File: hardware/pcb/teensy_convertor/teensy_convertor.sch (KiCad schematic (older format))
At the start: 2 parts, among them U1 Teensy-3.2

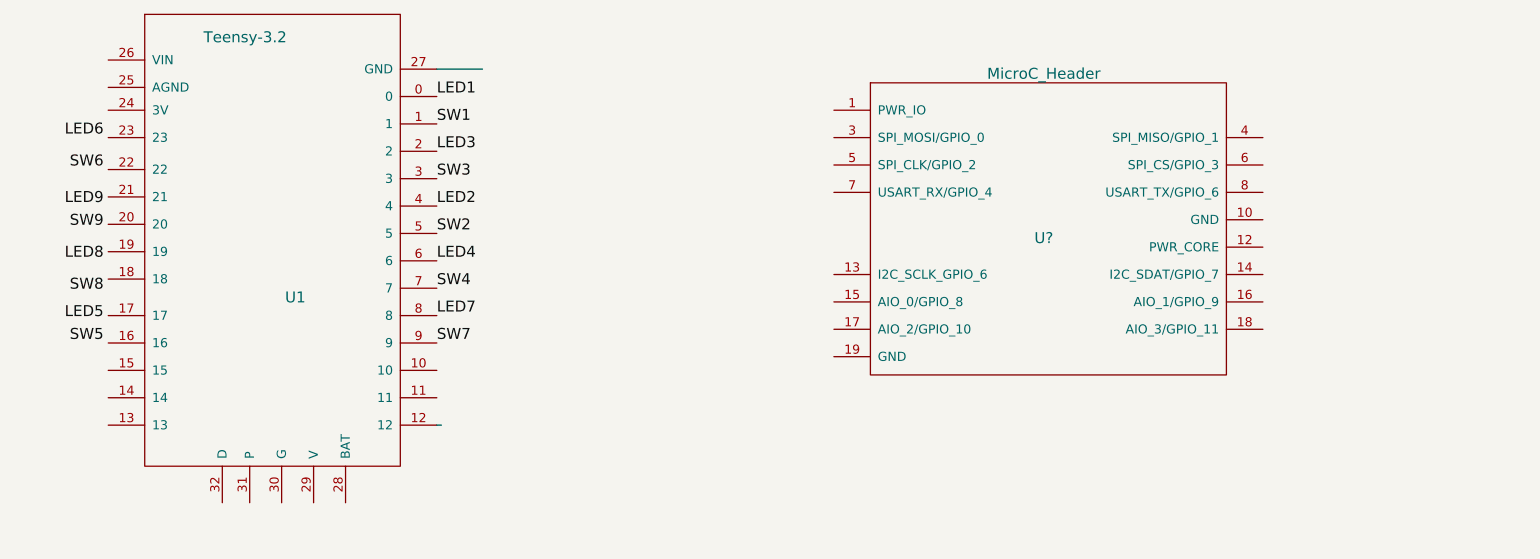
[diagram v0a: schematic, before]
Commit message: Add lables from Teensy to microcontroller header
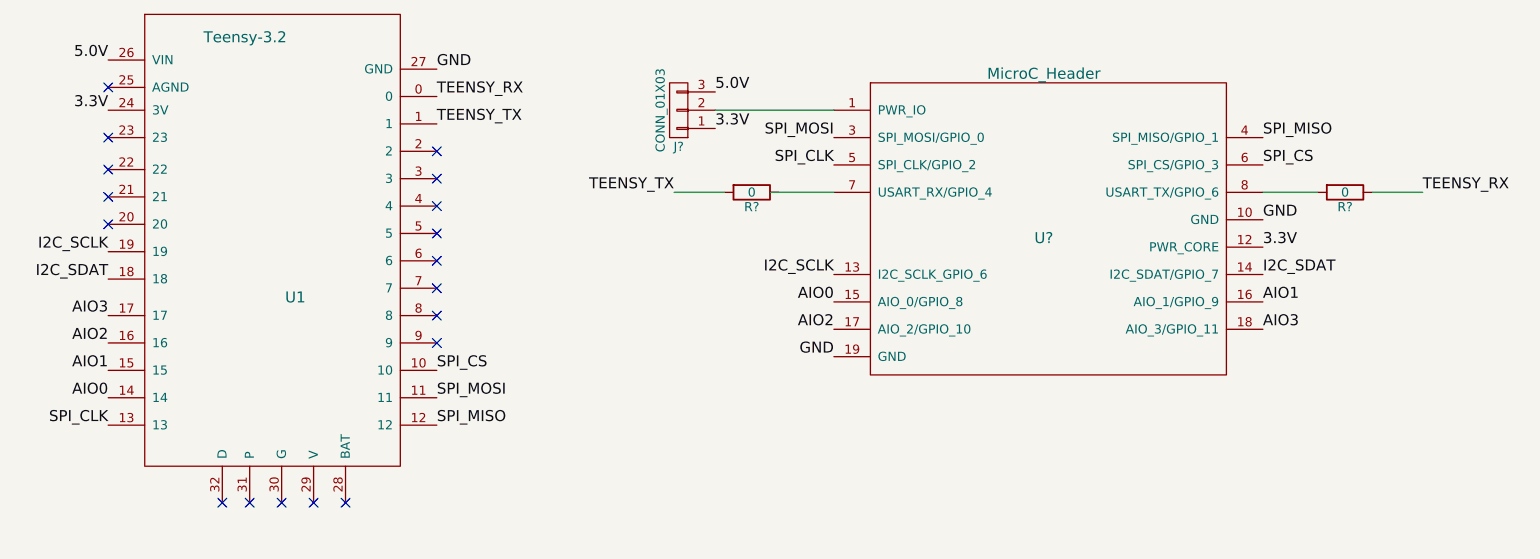
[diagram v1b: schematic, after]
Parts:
- added J?: CONN_01X03, symbol CONN_01X03
- added R? (x2): 0, symbol R
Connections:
- net labels added: 3.3V, 5.0V, AIO0, AIO1, AIO2, AIO3, GND, I2C_SCLK, I2C_SDAT, SPI_CLK, SPI_CS, SPI_MISO, SPI_MOSI, TEENSY_RX, TEENSY_TX
- net labels removed: LED1, LED2, LED3, LED4, LED5, LED6, LED7, LED8, LED9, SW1, SW2, SW3, SW4, SW5, SW6, SW7, SW8, SW9
- wire segments 2 -> 5
- no-connect marks 0 -> 18
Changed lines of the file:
@@
 LIBS:Zilog
 LIBS:micro_c_header
+LIBS:teensy_convertor-cache
 EELAYER 25 0
 EELAYER END
@@
 	1    0    0    -1
 $EndComp
-Wire Wire Line
-	4175 2625 3925 2625
-Wire Wire Line
-	3950 4575 3925 4575
-Text Label 3925 2775 0    60   ~ 0
-LED1
-Text Label 3925 2925 0    60   ~ 0
-SW1
-Text Label 3925 3075 0    60   ~ 0
-LED3
-Text Label 3925 3225 0    60   ~ 0
-SW3
-Text Label 3925 3375 0    60   ~ 0
-LED2
-Text Label 3925 3525 0    60   ~ 0
-SW2
-Text Label 2100 3000 2    60   ~ 0
-LED6
-Text Label 2100 3175 2    60   ~ 0
-SW6
-Text Label 2100 3375 2    60   ~ 0
-LED9
-Text Label 2100 3500 2    60   ~ 0
-SW9
-Text Label 2100 3675 2    60   ~ 0
-LED8
-Text Label 2100 3850 2    60   ~ 0
-SW8
-Text Label 3925 3675 0    60   ~ 0
-LED4
-Text Label 3925 3825 0    60   ~ 0
-SW4
-Text Label 3925 3975 0    60   ~ 0
-LED7
-Text Label 3925 4125 0    60   ~ 0
-SW7
-Text Label 2100 4000 2    60   ~ 0
-LED5
-Text Label 2100 4125 2    60   ~ 0
-SW5
 $Comp
 L MicroC_Header U?
@@
 	1    0    0    -1
 $EndComp
+$Comp
+L CONN_01X03 J?
+U 1 1 592B3FA3
+P 5250 2850
+F 0 "J?" H 5250 3050 50  0000 C CNN
+F 1 "CONN_01X03" V 5350 2850 50  0000 C CNN
+F 2 "" H 5250 2850 50  0001 C CNN
+F 3 "" H 5250 2850 50  0001 C CNN
+	1    5250 2850
+	-1   0    0    1
+$EndComp
+Text Label 2125 2850 2    60   ~ 0
+3.3V
+Text Label 5450 2950 0    60   ~ 0
+3.3V
+Text Label 8450 3600 0    60   ~ 0
+3.3V
+Text Label 2125 2575 2    60   ~ 0
+5.0V
+Text Label 5450 2750 0    60   ~ 0
+5.0V
+Text Label 8450 3450 0    60   ~ 0
+GND
+Text Label 6100 4200 2    60   ~ 0
+GND
+Text Label 3925 2625 0    60   ~ 0
+GND
+Text Label 6100 3000 2    60   ~ 0
+SPI_MOSI
+Text Label 3925 4425 0    60   ~ 0
+SPI_MOSI
+Text Label 6100 3150 2    60   ~ 0
+SPI_CLK
+Text Label 2125 4575 2    60   ~ 0
+SPI_CLK
+Text Label 8450 3000 0    60   ~ 0
+SPI_MISO
+Text Label 3925 4575 0    60   ~ 0
+SPI_MISO
+Text Label 8450 3150 0    60   ~ 0
+SPI_CS
+Text Label 3925 4275 0    60   ~ 0
+SPI_CS
+$Comp
+L R R?
+U 1 1 592B478D
+P 5650 3300
+F 0 "R?" V 5730 3300 50  0000 C CNN
+F 1 "0" V 5650 3300 50  0000 C CNN
+F 2 "" V 5580 3300 50  0001 C CNN
+F 3 "" H 5650 3300 50  0001 C CNN
+	1    5650 3300
+	0    1    1    0
+$EndComp
+$Comp
+L R R?
+U 1 1 592B4823
+P 8900 3300
+F 0 "R?" V 8980 3300 50  0000 C CNN
+F 1 "0" V 8900 3300 50  0000 C CNN
+F 2 "" V 8830 3300 50  0001 C CNN
+F 3 "" H 8900 3300 50  0001 C CNN
+	1    8900 3300
+	0    1    1    0
+$EndComp
+Wire Wire Line
+	6100 2850 5450 2850
+Wire Wire Line
+	5750 3300 6100 3300
+Wire Wire Line
+	8450 3300 8750 3300
+Wire Wire Line
+	9050 3300 9325 3300
+Wire Wire Line
+	5500 3300 5225 3300
+Text Label 9325 3300 0    60   ~ 0
+TEENSY_RX
+Text Label 3925 2775 0    60   ~ 0
+TEENSY_RX
+Text Label 5225 3300 2    60   ~ 0
+TEENSY_TX
+Text Label 3925 2925 0    60   ~ 0
+TEENSY_TX
+Text Label 6100 3750 2    60   ~ 0
+I2C_SCLK
+Text Label 2125 3625 2    60   ~ 0
+I2C_SCLK
+Text Label 2125 3775 2    60   ~ 0
+I2C_SDAT
+Text Label 8450 3750 0    60   ~ 0
+I2C_SDAT
+Text Label 6100 3900 2    60   ~ 0
+AIO0
+Text Label 2125 4425 2    60   ~ 0
+AIO0
+Text Label 6100 4050 2    60   ~ 0
+AIO2
+Text Label 8450 3900 0    60   ~ 0
+AIO1
+Text Label 8450 4050 0    60   ~ 0
+AIO3
+Text Label 2125 4125 2    60   ~ 0
+AIO2
+Text Label 2125 4275 2    60   ~ 0
+AIO1
+Text Label 2125 3975 2    60   ~ 0
+AIO3
+NoConn ~ 3925 3075
+NoConn ~ 3925 3225
+NoConn ~ 3925 3375
+NoConn ~ 3925 3525
+NoConn ~ 3925 3675
+NoConn ~ 3925 3825
+NoConn ~ 3925 3975
+NoConn ~ 3925 4125
+NoConn ~ 3425 5000
+NoConn ~ 3250 5000
+NoConn ~ 3075 5000
+NoConn ~ 2900 5000
+NoConn ~ 2750 5000
+NoConn ~ 2125 3475
+NoConn ~ 2125 3325
+NoConn ~ 2125 3175
+NoConn ~ 2125 3000
+NoConn ~ 2125 2725
 $EndSCHEMATC

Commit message: Initial association and import into the layout tool
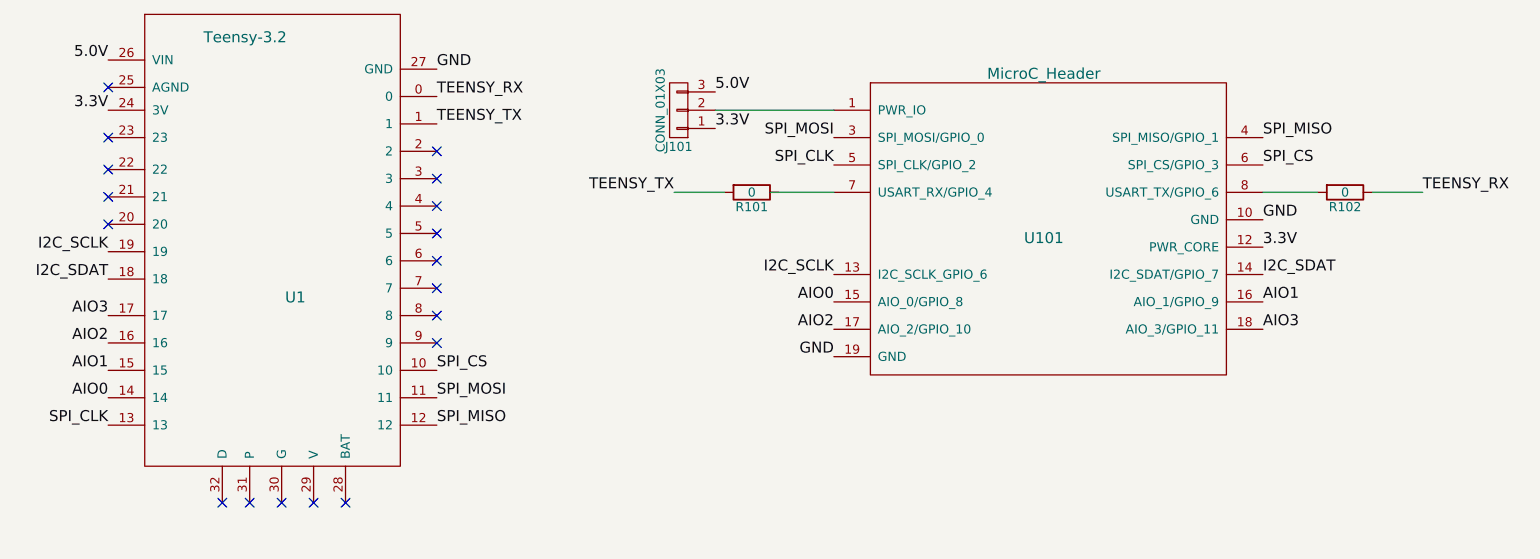
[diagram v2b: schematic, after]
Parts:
- J101: renamed from J?; footprint (none) -> Pin_Headers:Pin_Header_Straight_1x03_Pitch2.54mm
- R101, R102: renamed from R?; footprint (none) -> Resistors_SMD:R_0805_HandSoldering
- U1: footprint Key:Teensy-32 -> teensy_convertor:Teensy-32
- U101: renamed from U?; footprint (none) -> micro_c_header:MicroC_Header_Pitch2.54mm
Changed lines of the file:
@@
 F 0 "U1" H 3150 3375 60  0000 C CNN
 F 1 "Teensy-3.2" H 2875 4800 60  0000 C CNN
-F 2 "Key:Teensy-32" H 2775 3300 60  0001 C CNN
+F 2 "teensy_convertor:Teensy-32" H 2775 3300 60  0001 C CNN
 F 3 "" H 2775 3300 60  0001 C CNN
 	1    3000 3625
@@
 $EndComp
 $Comp
-L MicroC_Header U?
+L MicroC_Header U101
 U 1 1 59279C22
 P 7250 3550
-F 0 "U?" H 7250 3550 60  0000 C CNN
+F 0 "U101" H 7250 3550 60  0000 C CNN
 F 1 "MicroC_Header" H 7250 4450 60  0000 C CNN
-F 2 "" H 7250 3400 60  0001 C CNN
+F 2 "micro_c_header:MicroC_Header_Pitch2.54mm" H 7250 3400 60  0001 C CNN
 F 3 "" H 7250 3400 60  0001 C CNN
 	1    7250 3550
@@
 $EndComp
 $Comp
-L CONN_01X03 J?
+L CONN_01X03 J101
 U 1 1 592B3FA3
 P 5250 2850
-F 0 "J?" H 5250 3050 50  0000 C CNN
+F 0 "J101" H 5250 3050 50  0000 C CNN
 F 1 "CONN_01X03" V 5350 2850 50  0000 C CNN
-F 2 "" H 5250 2850 50  0001 C CNN
+F 2 "Pin_Headers:Pin_Header_Straight_1x03_Pitch2.54mm" H 5250 2850 50  0001 C CNN
 F 3 "" H 5250 2850 50  0001 C CNN
 	1    5250 2850
@@
 SPI_CS
 $Comp
-L R R?
+L R R101
 U 1 1 592B478D
 P 5650 3300
-F 0 "R?" V 5730 3300 50  0000 C CNN
+F 0 "R101" V 5730 3300 50  0000 C CNN
 F 1 "0" V 5650 3300 50  0000 C CNN
-F 2 "" V 5580 3300 50  0001 C CNN
+F 2 "Resistors_SMD:R_0805_HandSoldering" V 5580 3300 50  0001 C CNN
 F 3 "" H 5650 3300 50  0001 C CNN
 	1    5650 3300
@@
 $EndComp
 $Comp
-L R R?
+L R R102
 U 1 1 592B4823
 P 8900 3300
-F 0 "R?" V 8980 3300 50  0000 C CNN
+F 0 "R102" V 8980 3300 50  0000 C CNN
 F 1 "0" V 8900 3300 50  0000 C CNN
-F 2 "" V 8830 3300 50  0001 C CNN
+F 2 "Resistors_SMD:R_0805_HandSoldering" V 8830 3300 50  0001 C CNN
 F 3 "" H 8900 3300 50  0001 C CNN
 	1    8900 3300

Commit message: Initial layout
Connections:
- no-connect marks 18 -> 17
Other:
- moved on the sheet: U1
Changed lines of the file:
@@
 L Teensy-3.2 U1
 U 1 1 586B0354
-P 3000 3625
-F 0 "U1" H 3150 3375 60  0000 C CNN
-F 1 "Teensy-3.2" H 2875 4800 60  0000 C CNN
-F 2 "teensy_convertor:Teensy-32" H 2775 3300 60  0001 C CNN
-F 3 "" H 2775 3300 60  0001 C CNN
-	1    3000 3625
-	1    0    0    -1
+P 3100 3625
+F 0 "U1" H 3250 3375 60  0000 C CNN
+F 1 "Teensy-3.2" H 2975 4800 60  0000 C CNN
+F 2 "teensy_convertor:Teensy-32" H 2875 3300 60  0001 C CNN
+F 3 "" H 2875 3300 60  0001 C CNN
+	1    3100 3625
+	-1   0    0    -1
 $EndComp
 $Comp
@@
 	-1   0    0    1
 $EndComp
-Text Label 2125 2850 2    60   ~ 0
+Text Label 3975 2850 0    60   ~ 0
 3.3V
 Text Label 5450 2950 0    60   ~ 0
@@
 Text Label 8450 3600 0    60   ~ 0
 3.3V
-Text Label 2125 2575 2    60   ~ 0
+Text Label 3975 2575 0    60   ~ 0
 5.0V
 Text Label 5450 2750 0    60   ~ 0
@@
 Text Label 6100 4200 2    60   ~ 0
 GND
-Text Label 3925 2625 0    60   ~ 0
+Text Label 2175 2625 2    60   ~ 0
 GND
 Text Label 6100 3000 2    60   ~ 0
 SPI_MOSI
-Text Label 3925 4425 0    60   ~ 0
+Text Label 2175 4425 2    60   ~ 0
 SPI_MOSI
 Text Label 6100 3150 2    60   ~ 0
 SPI_CLK
-Text Label 2125 4575 2    60   ~ 0
+Text Label 3975 4575 0    60   ~ 0
 SPI_CLK
 Text Label 8450 3000 0    60   ~ 0
 SPI_MISO
-Text Label 3925 4575 0    60   ~ 0
+Text Label 2175 4575 2    60   ~ 0
 SPI_MISO
 Text Label 8450 3150 0    60   ~ 0
 SPI_CS
-Text Label 3925 4275 0    60   ~ 0
+Text Label 2175 4275 2    60   ~ 0
 SPI_CS
 $Comp
@@
 	6100 2850 5450 2850
 Wire Wire Line
-	5750 3300 6100 3300
+	5800 3300 6100 3300
 Wire Wire Line
 	8450 3300 8750 3300
@@
 Text Label 9325 3300 0    60   ~ 0
 TEENSY_RX
-Text Label 3925 2775 0    60   ~ 0
+Text Label 2175 2775 2    60   ~ 0
 TEENSY_RX
 Text Label 5225 3300 2    60   ~ 0
 TEENSY_TX
-Text Label 3925 2925 0    60   ~ 0
+Text Label 2175 2925 2    60   ~ 0
 TEENSY_TX
 Text Label 6100 3750 2    60   ~ 0
 I2C_SCLK
-Text Label 2125 3625 2    60   ~ 0
+Text Label 3975 3625 0    60   ~ 0
 I2C_SCLK
-Text Label 2125 3775 2    60   ~ 0
+Text Label 3975 3775 0    60   ~ 0
 I2C_SDAT
 Text Label 8450 3750 0    60   ~ 0
@@
 Text Label 6100 3900 2    60   ~ 0
 AIO0
-Text Label 2125 4425 2    60   ~ 0
+Text Label 3975 4425 0    60   ~ 0
 AIO0
 Text Label 6100 4050 2    60   ~ 0
@@
 Text Label 8450 4050 0    60   ~ 0
 AIO3
-Text Label 2125 4125 2    60   ~ 0
+Text Label 3975 4125 0    60   ~ 0
 AIO2
-Text Label 2125 4275 2    60   ~ 0
+Text Label 3975 4275 0    60   ~ 0
 AIO1
-Text Label 2125 3975 2    60   ~ 0
+Text Label 3975 3975 0    60   ~ 0
 AIO3
-NoConn ~ 3925 3075
-NoConn ~ 3925 3225
-NoConn ~ 3925 3375
-NoConn ~ 3925 3525
-NoConn ~ 3925 3675
-NoConn ~ 3925 3825
-NoConn ~ 3925 3975
-NoConn ~ 3925 4125
-NoConn ~ 3425 5000
-NoConn ~ 3250 5000
-NoConn ~ 3075 5000
-NoConn ~ 2900 5000
-NoConn ~ 2750 5000
-NoConn ~ 2125 3475
-NoConn ~ 2125 3325
-NoConn ~ 2125 3175
-NoConn ~ 2125 3000
-NoConn ~ 2125 2725
+NoConn ~ 2175 3075
+NoConn ~ 2175 3225
+NoConn ~ 2175 3375
+NoConn ~ 2175 3525
+NoConn ~ 2175 3675
+NoConn ~ 2175 3825
+NoConn ~ 2175 3975
+NoConn ~ 2175 4125
+NoConn ~ 2675 5000
+NoConn ~ 2850 5000
+NoConn ~ 3200 5000
+NoConn ~ 3350 5000
+NoConn ~ 3975 3475
+NoConn ~ 3975 3325
+NoConn ~ 3975 3175
+NoConn ~ 3975 3000
+NoConn ~ 3975 2725
+Text Label 3025 5000 3    60   ~ 0
+GND
 $EndSCHEMATC

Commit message: Minor update to the schematic
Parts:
- renumbered U1 to U101, U101 to U102
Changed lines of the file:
@@
 $EndDescr
 $Comp
-L Teensy-3.2 U1
+L Teensy-3.2 U101
 U 1 1 586B0354
 P 3100 3625
-F 0 "U1" H 3250 3375 60  0000 C CNN
+F 0 "U101" H 3250 3375 60  0000 C CNN
 F 1 "Teensy-3.2" H 2975 4800 60  0000 C CNN
 F 2 "teensy_convertor:Teensy-32" H 2875 3300 60  0001 C CNN
@@
 $EndComp
 $Comp
-L MicroC_Header U101
+L MicroC_Header U102
 U 1 1 59279C22
 P 7250 3550
-F 0 "U101" H 7250 3550 60  0000 C CNN
+F 0 "U102" H 7250 3550 60  0000 C CNN
 F 1 "MicroC_Header" H 7250 4450 60  0000 C CNN
 F 2 "micro_c_header:MicroC_Header_Pitch2.54mm" H 7250 3400 60  0001 C CNN
